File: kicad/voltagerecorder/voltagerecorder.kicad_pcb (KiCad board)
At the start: 2 copper layers, 82 parts, among them J1 Conn_02x10_Odd_Even, J2 Phoenix Stecker, J3 Conn_02x08_Odd_Even, J4 Conn_01x01_Male, J5 Conn_01x01_Male, J6 Conn_01x01_Male, J7 Conn_01x01_Male, U1 Opamp_Quad, U2 DCDC_BIPOLAR, U3 L78L12ACUTR, U4 L79L12ACUTR, U5 ADS8638

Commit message: placing finished
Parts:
- removed R32, R33: nc, Resistor_SMD:R_0603_1608Metric_Pad0.98x0.95mm_HandSolder
- C11, C15, C16, C17, C18, C2, C22, C4, C6, U3, U4: moved to B.Cu
- C14: footprint Capacitor_SMD:C_0603_1608Metric_Pad1.08x0.95mm_HandSolder -> Capacitor_SMD:C_0805_2012Metric_Pad1.18x1.45mm_HandSolder
- J3: value Conn_02x08_Odd_Even -> Conn_01x08; footprint Connector_PinHeader_2.54mm:PinHeader_2x08_P2.54mm_Vertical -> Connector_PinHeader_2.54mm:PinHeader_1x08_P2.54mm_Vertical
- moved R17 97.4 mm to (144.0, 96.0), turned to 180 degrees
- moved R24 95.9 mm to (151.4, 99.1), turned to 180 degrees
- moved R31 93.3 mm to (151.4, 85.9), turned to 180 degrees
- moved R16 92.2 mm to (146.0, 97.5), turned to 180 degrees
- moved R23 90.7 mm to (151.4, 97.5)
- moved R30 88.1 mm to (151.4, 87.4)
- moved R10 86.7 mm to (144.0, 88.9), turned to 180 degrees
- moved R9 84.8 mm to (146.0, 87.4), turned to 180 degrees
- moved J5 83.6 mm to (135.0, 104.7)
- moved R7 81.6 mm to (135.0, 96.2), turned to -90 degrees
- moved R8 81.3 mm to (139.5, 96.7), turned to -90 degrees
- moved R14 79.8 mm to (135.0, 109.3), turned to -90 degrees
- moved J4 79.4 mm to (135.0, 91.6)
- moved R15 79.1 mm to (139.5, 109.8), turned to -90 degrees
- moved D1 77.5 mm to (138.5, 92.6), turned to -90 degrees
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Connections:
- J3 pad 2: /SCLK -> /MOSI
- J3 pad 3: /MOSI -> /MISO
- J3 pad 4: /MOSI -> /CS
- J3 pad 5: /MISO -> /PD
- J3 pad 6: /MISO -> +3.3V
- J3 pad 7: /CS -> +5V
- J3 pad 8: /CS -> GND
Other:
- board outline added: 72.1 x 47.8 mm

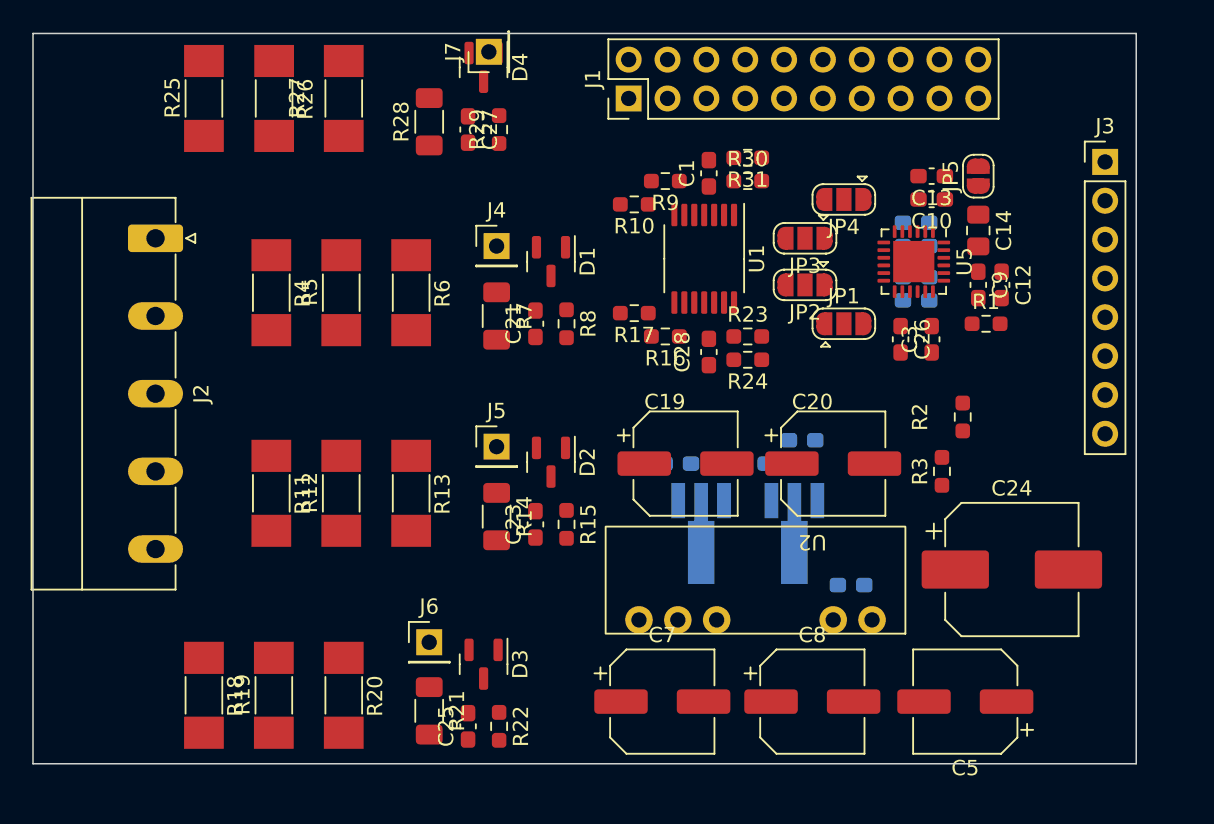
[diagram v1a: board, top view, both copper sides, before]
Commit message: Rasterversatz korrigiert.
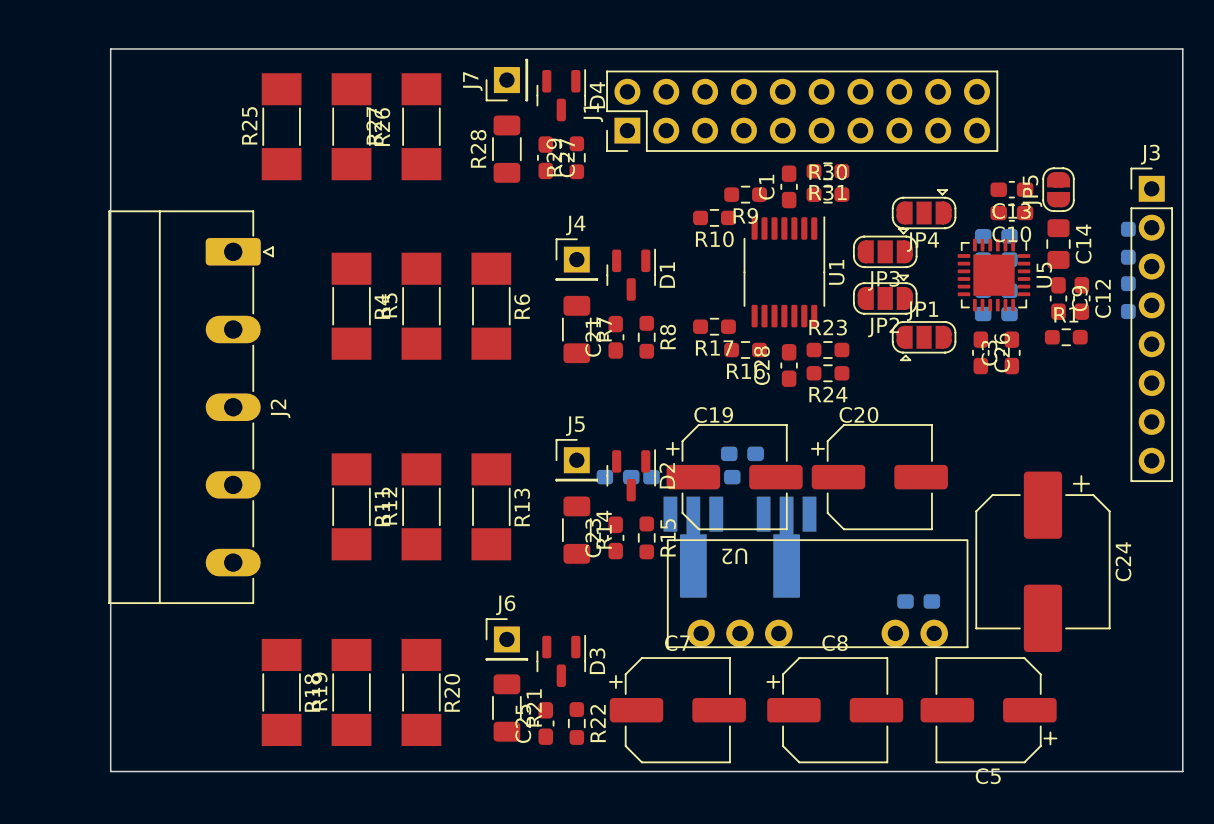
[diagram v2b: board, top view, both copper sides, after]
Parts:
- R2, R3: moved to B.Cu
- moved R3 16.7 mm to (176.3, 95.0)
- moved R2 15.7 mm to (176.3, 91.4)
- moved R29 5.41 mm to (140.2, 85.9)
- moved D4 5.41 mm to (139.2, 81.8)
- moved R25 5.41 mm to (120.9, 83.8)
- moved R27 5.41 mm to (130.0, 83.8)
- moved C27 5.41 mm to (138.2, 85.9)
- moved R26 5.39 mm to (125.5, 83.8)
- moved R28 5.39 mm to (135.6, 85.3)
- moved C1 5.32 mm to (154.1, 87.8)
- moved C12 5.32 mm to (173.2, 95.1)
- moved C14 5.32 mm to (171.7, 91.5)
- moved C23 5.32 mm to (142.7, 110.7)
- moved C9 5.32 mm to (171.7, 95.1)
- moved D1 5.32 mm to (143.8, 93.5)
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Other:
- board size 72.1 x 47.8 mm -> 70.1 x 47.2 mm

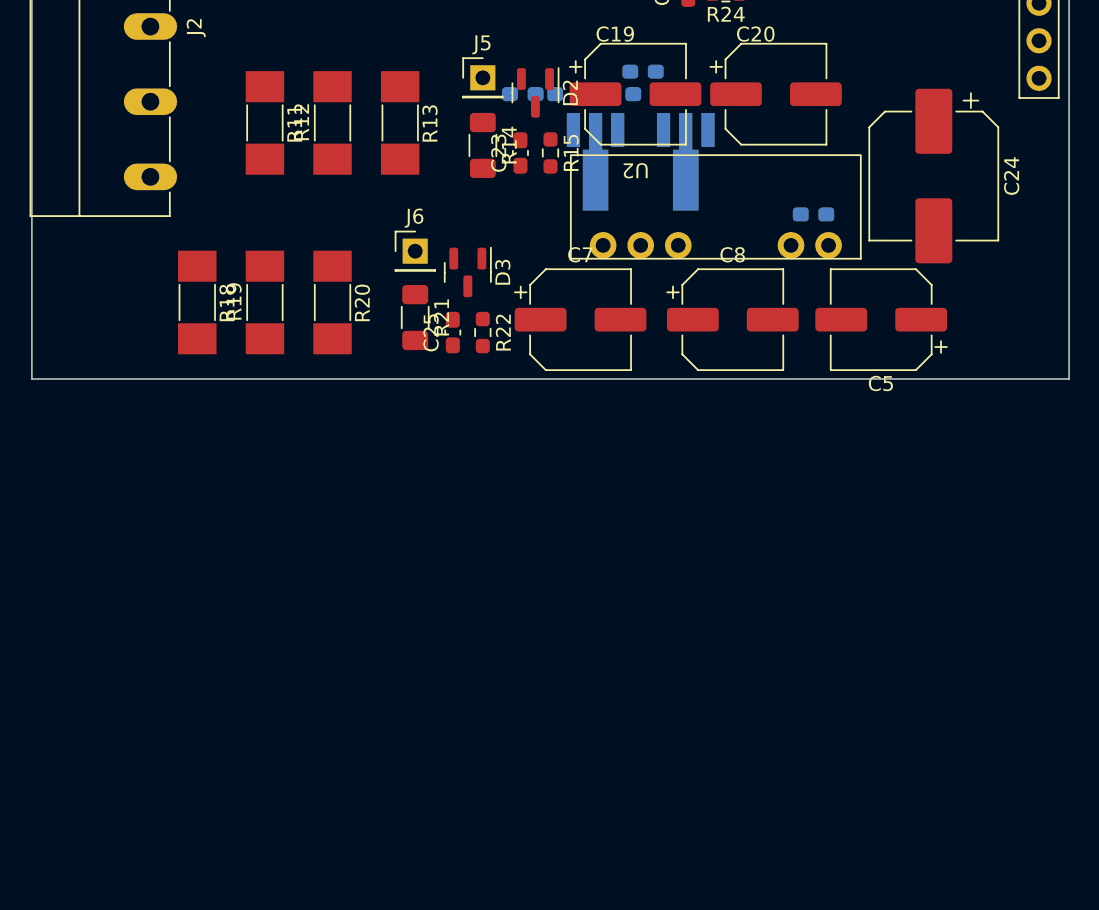
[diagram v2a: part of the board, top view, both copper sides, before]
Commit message: ESP32-S3 WROOM 2 hinzugefügt.
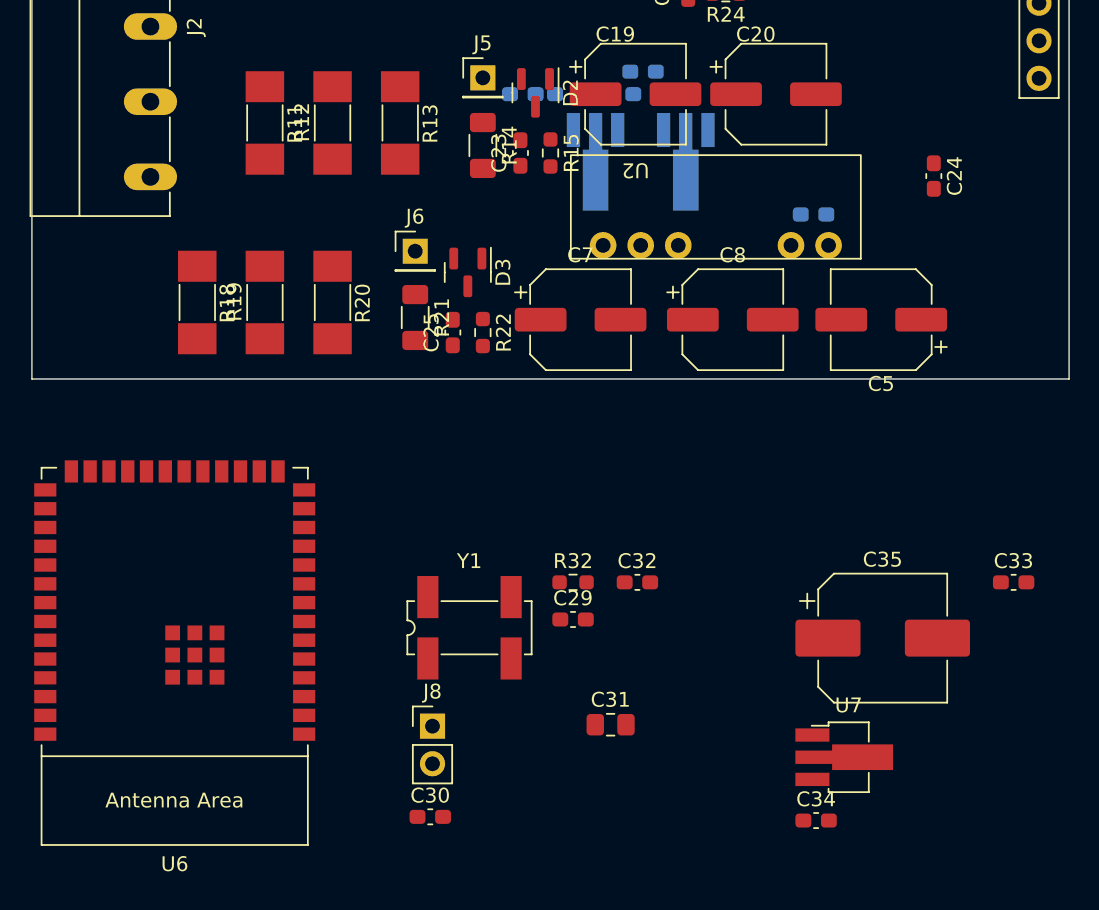
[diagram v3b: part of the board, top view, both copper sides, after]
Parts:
- added C29: 12p, Capacitor_SMD:C_0603_1608Metric_Pad1.08x0.95mm_HandSolder, F.Cu at (146.3, 142.2)
- added C30: 100n, Capacitor_SMD:C_0603_1608Metric_Pad1.08x0.95mm_HandSolder, F.Cu at (136.7, 155.6)
- added C31: 10u, Capacitor_SMD:C_0805_2012Metric_Pad1.18x1.45mm_HandSolder, F.Cu at (148.8, 149.4)
- added C32: 100n, Capacitor_SMD:C_0603_1608Metric_Pad1.08x0.95mm_HandSolder, F.Cu at (150.7, 139.7)
- added C33: 100n, Capacitor_SMD:C_0603_1608Metric_Pad1.08x0.95mm_HandSolder, F.Cu at (176.1, 139.7)
- added C34: 100n, Capacitor_SMD:C_0603_1608Metric_Pad1.08x0.95mm_HandSolder, F.Cu at (162.7, 155.8)
- added C35: 470u, Capacitor_SMD:CP_Elec_8x10.5, F.Cu at (167.2, 143.5)
- added J8: Conn_01x02, Connector_PinHeader_2.54mm:PinHeader_1x02_P2.54mm_Vertical, F.Cu at (136.8, 149.4)
- added R32: 10k, Resistor_SMD:R_0603_1608Metric_Pad0.98x0.95mm_HandSolder, F.Cu at (146.3, 139.7)
- added U6: ESP32-S3-WROOM-2, Espressif:ESP32-S3-WROOM-2, F.Cu at (119.4, 141.7)
- added U7: L78L12ACUTR, Package_TO_SOT_SMD:SOT-89-3_Handsoldering, F.Cu at (164.6, 151.6)
- added Y1: 32.768kHz, Crystal:Crystal_SMD_SeikoEpson_MC306-4Pin_8.0x3.2mm_HandSoldering, F.Cu at (139.3, 142.8)
- C24: value 470u -> 12p; footprint Capacitor_SMD:CP_Elec_8x10.5 -> Capacitor_SMD:C_0603_1608Metric_Pad1.08x0.95mm_HandSolder
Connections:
- C24 pad 1: +3.3V -> Net-(C24-Pad1)

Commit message: sd card hinzugefügt
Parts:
- added J9: Micro_SD_Card, Connector_Card:microSD_HC_Hirose_DM3BT-DSF-PEJS, F.Cu at (187.5, 148.8)
- Y1: value 32.768kHz -> Crystal_GND23
- moved R3 8.77 mm to (174.8, 103.6)
- moved R2 8.77 mm to (174.8, 100.1)
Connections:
- Y1 pad 1: Net-(C24-Pad1) -> Net-(C29-Pad1)
- Y1 pad 2: Net-(C29-Pad1) -> unconnected-(Y1-Pad2)
- Y1 pad 3: (no net) -> unconnected-(Y1-Pad3)
- Y1 pad 4: (no net) -> Net-(C24-Pad1)

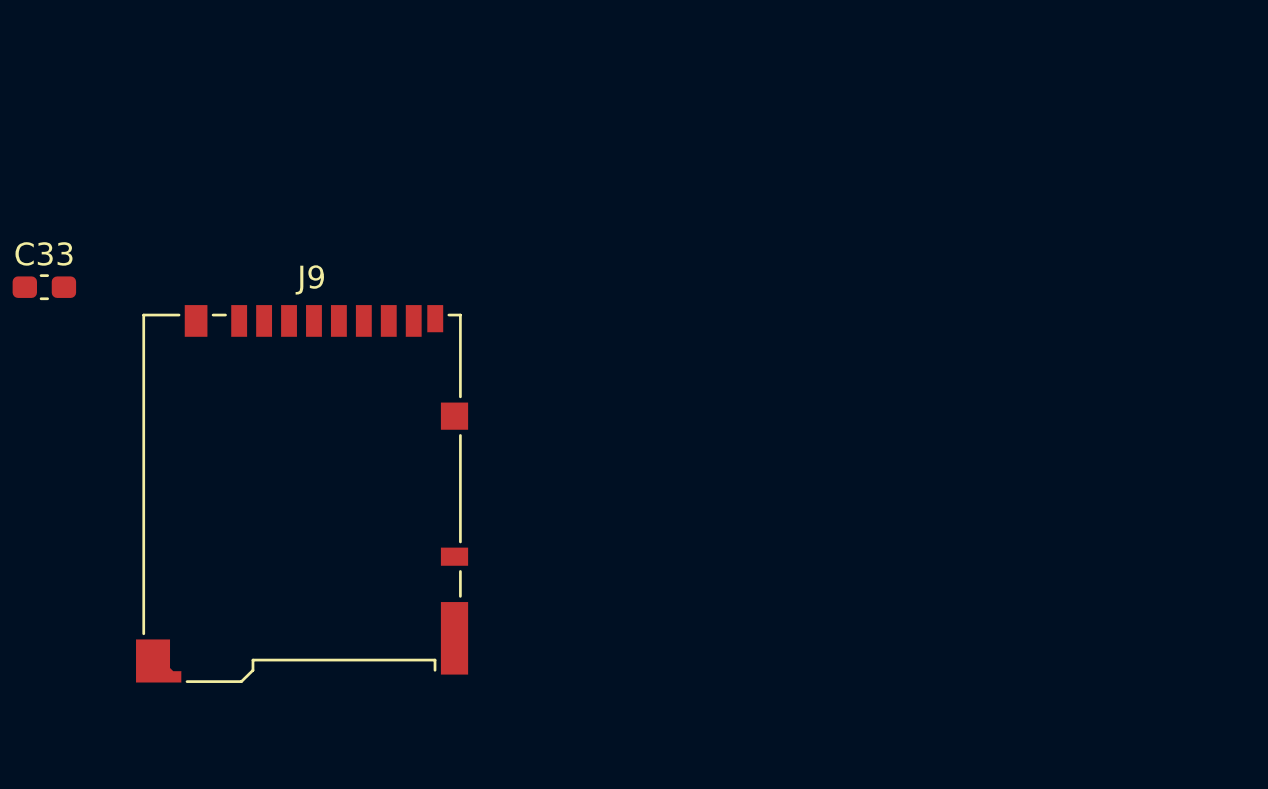
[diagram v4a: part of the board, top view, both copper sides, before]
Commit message: SD und USB-C added.
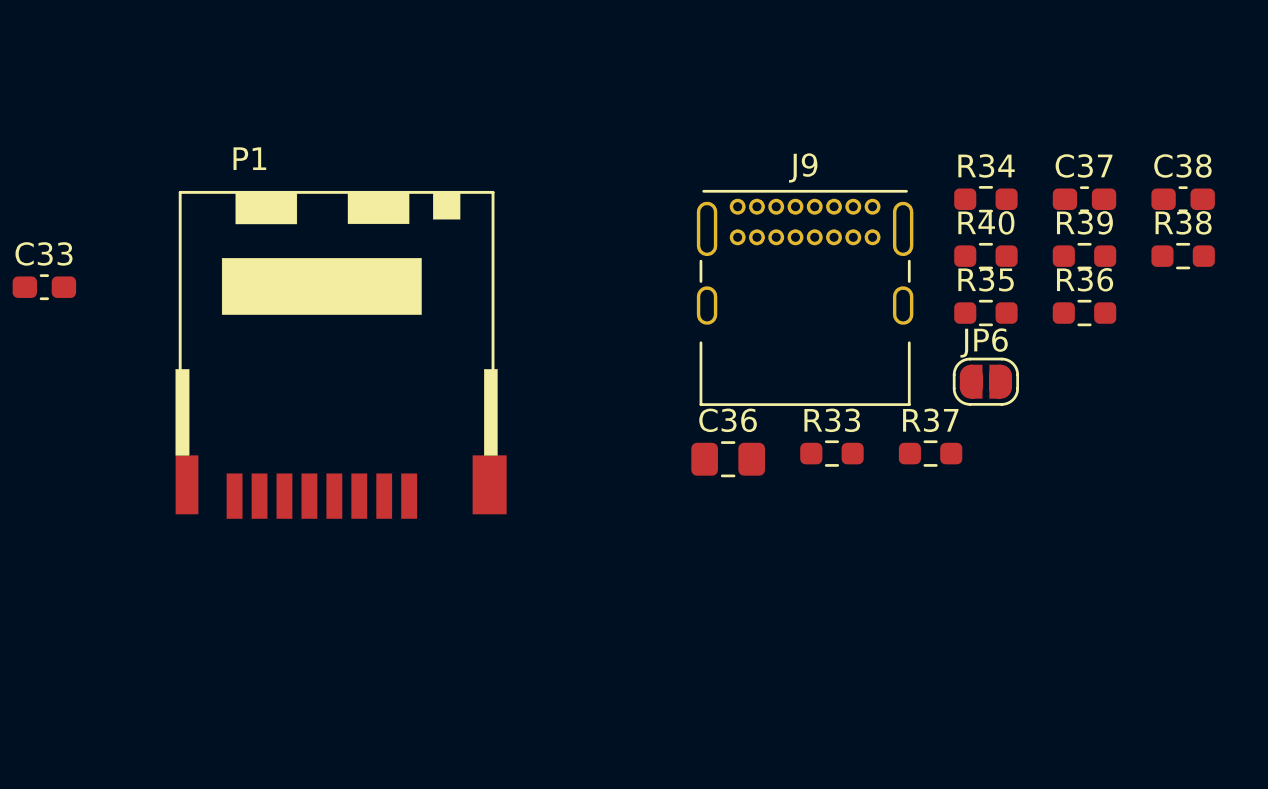
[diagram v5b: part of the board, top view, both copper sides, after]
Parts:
- added C36: 10u, Capacitor_SMD:C_0805_2012Metric_Pad1.18x1.45mm_HandSolder, F.Cu at (206.2, 147.3)
- added C37: 100n, Capacitor_SMD:C_0603_1608Metric_Pad1.08x0.95mm_HandSolder, F.Cu at (222.0, 135.8)
- added C38: 100n, Capacitor_SMD:C_0603_1608Metric_Pad1.08x0.95mm_HandSolder, F.Cu at (226.3, 135.8)
- added JP6: SolderJumper_2_Open, Jumper:SolderJumper-2_P1.3mm_Open_RoundedPad1.0x1.5mm, F.Cu at (217.6, 143.9)
- added P1: DM3CS-SF, Hirose:HRS_DM3CS-SF, F.Cu at (189.0, 142.7)
- added R33: 10k, Resistor_SMD:R_0603_1608Metric_Pad0.98x0.95mm_HandSolder, F.Cu at (210.8, 147.1)
- added R34: 10k, Resistor_SMD:R_0603_1608Metric_Pad0.98x0.95mm_HandSolder, F.Cu at (217.6, 135.8)
- added R35: 10k, Resistor_SMD:R_0603_1608Metric_Pad0.98x0.95mm_HandSolder, F.Cu at (217.6, 140.9)
- added R36: 10k, Resistor_SMD:R_0603_1608Metric_Pad0.98x0.95mm_HandSolder, F.Cu at (222.0, 140.9)
- added R37: 10k, Resistor_SMD:R_0603_1608Metric_Pad0.98x0.95mm_HandSolder, F.Cu at (215.2, 147.1)
- added R38: 10k, Resistor_SMD:R_0603_1608Metric_Pad0.98x0.95mm_HandSolder, F.Cu at (226.3, 138.4)
- added R39: 10k, Resistor_SMD:R_0603_1608Metric_Pad0.98x0.95mm_HandSolder, F.Cu at (222.0, 138.4)
- added R40: 15k, Resistor_SMD:R_0603_1608Metric_Pad0.98x0.95mm_HandSolder, F.Cu at (217.6, 138.4)
- J9: value Micro_SD_Card -> USB_C_Receptacle_USB2.0; footprint Connector_Card:microSD_HC_Hirose_DM3BT-DSF-PEJS -> Connector_USB:USB_C_Receptacle_GCT_USB4085
- moved J9 23.0 mm to (206.7, 136.2)
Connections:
- J3 pad 5: /PD -> /AL_PD
- U6 pad 13: unconnected-(U6-Pad13) -> Net-(U6-Pad13)
- U6 pad 14: unconnected-(U6-Pad14) -> Net-(U6-Pad14)
- U6 pad 15: unconnected-(U6-Pad15) -> Net-(U6-Pad15)
- U6 pad 17: unconnected-(U6-Pad17) -> /AL_PD
- U6 pad 38: unconnected-(U6-Pad38) -> Net-(P1-Pad3)
- U6 pad 39: unconnected-(U6-Pad39) -> Net-(U6-Pad39)
- U6 pad 4: unconnected-(U6-Pad4) -> Net-(U6-Pad4)
- U6 pad 5: unconnected-(U6-Pad5) -> Net-(U6-Pad5)
- U6 pad 6: unconnected-(U6-Pad6) -> Net-(U6-Pad6)
- U6 pad 7: /PD -> Net-(U6-Pad7)

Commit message: a
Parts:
- added U8: ESP32-C3-WROOM-02, Espressif:ESP32-C3-WROOM-02, F.Cu at (101.1, 149.4)
- U6: value ESP32-S3-WROOM-2 -> STM32G473CBT6; footprint Espressif:ESP32-S3-WROOM-2 -> Package_QFP:LQFP-48_7x7mm_P0.5mm
- moved U6 4.10 mm to (123.4, 142.2)
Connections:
- C38 pad 1: Net-(U6-Pad39) -> Net-(C38-Pad1)
- J8 pad 1: Net-(J8-Pad1) -> unconnected-(J8-Pad1)
- J9 pad A6: Net-(U6-Pad14) -> Net-(J9-PadA6)
- J9 pad A7: Net-(U6-Pad13) -> Net-(J9-PadA7)
- J9 pad B6: Net-(U6-Pad14) -> Net-(J9-PadA6)
- J9 pad B7: Net-(U6-Pad13) -> Net-(J9-PadA7)
- P1 pad 1: Net-(U6-Pad6) -> Net-(P1-Pad1)
- P1 pad 2: Net-(U6-Pad7) -> Net-(P1-Pad2)
- P1 pad 5: Net-(U6-Pad15) -> Net-(P1-Pad5)
- P1 pad 7: Net-(U6-Pad4) -> Net-(P1-Pad7)
- P1 pad 8: Net-(U6-Pad5) -> Net-(P1-Pad8)
- R34 pad 1: Net-(U6-Pad15) -> Net-(P1-Pad5)
- R35 pad 1: Net-(U6-Pad4) -> Net-(P1-Pad7)
- R36 pad 1: Net-(U6-Pad5) -> Net-(P1-Pad8)
- R37 pad 1: Net-(U6-Pad6) -> Net-(P1-Pad1)
- R38 pad 1: Net-(U6-Pad7) -> Net-(P1-Pad2)
- R39 pad 1: Net-(U6-Pad39) -> Net-(C38-Pad1)
- R40 pad 2: Net-(U6-Pad39) -> Net-(C38-Pad1)
- U6 pad 1: Net-(U6-Pad1) -> unconnected-(U6-Pad1)
- U6 pad 13: Net-(U6-Pad13) -> unconnected-(U6-Pad13)
- U6 pad 14: Net-(U6-Pad14) -> unconnected-(U6-Pad14)
- U6 pad 15: Net-(U6-Pad15) -> unconnected-(U6-Pad15)
- U6 pad 17: /AL_PD -> unconnected-(U6-Pad17)
- U6 pad 18: /CS -> unconnected-(U6-Pad18)
- U6 pad 19: /MOSI -> unconnected-(U6-Pad19)
- U6 pad 2: Net-(C31-Pad1) -> unconnected-(U6-Pad2)
- U6 pad 20: /SCLK -> unconnected-(U6-Pad20)
- U6 pad 21: /MISO -> unconnected-(U6-Pad21)
- U6 pad 27: Net-(J8-Pad1) -> unconnected-(U6-Pad27)
- U6 pad 3: Net-(C30-Pad1) -> unconnected-(U6-Pad3)
- U6 pad 38: Net-(P1-Pad3) -> unconnected-(U6-Pad38)
- U6 pad 39: Net-(U6-Pad39) -> unconnected-(U6-Pad39)
- U6 pad 4: Net-(U6-Pad4) -> unconnected-(U6-Pad4)
- U6 pad 40: Net-(U6-Pad1) -> unconnected-(U6-Pad40)
- U6 pad 41: Net-(U6-Pad1) -> unconnected-(U6-Pad41)
- U6 pad 5: Net-(U6-Pad5) -> unconnected-(U6-Pad5)
- U6 pad 6: Net-(U6-Pad6) -> unconnected-(U6-Pad6)
- U6 pad 7: Net-(U6-Pad7) -> unconnected-(U6-Pad7)
- U6 pad 8: Net-(C24-Pad1) -> unconnected-(U6-Pad8)
- U6 pad 9: Net-(C29-Pad1) -> unconnected-(U6-Pad9)
